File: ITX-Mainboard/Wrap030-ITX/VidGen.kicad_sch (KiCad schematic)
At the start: 26 parts, among them J1 Conn_02x05_Odd_Even, X2 25.175M

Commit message: Schematic substantial completion
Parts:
- added J3: DE15_Receptacle_HighDensity_MountingHoles, Wrap030-ITX:DE15-HD, symbol Connector:DE15_Receptacle_HighDensity_MountingHoles
- C1: footprint Capacitor_SMD:C_0805_2012Metric -> Capacitor_SMD:C_0402_1005Metric_Pad0.74x0.62mm_HandSolder; JLC-Part (none) -> https://jlcpcb.com/partdetail/1877-CL05B104KO5NNNC/C1525
- C15: footprint Capacitor_SMD:C_0805_2012Metric -> Capacitor_SMD:C_0402_1005Metric_Pad0.74x0.62mm_HandSolder; JLC-Part (none) -> https://jlcpcb.com/partdetail/53938-CL05A105KA5NQNC/C52923
- J1: footprint (none) -> Connector_PinHeader_2.54mm:PinHeader_2x05_P2.54mm_Vertical
- RN1, RN2, RN3, RN4, RN5, RN6: Mouser-Part (none) -> 603-YC164-FR-071KL; Notes (none) -> 1k x4
- RN7: Mouser-Part (none) -> 603-YC164-FR-0775RL; Notes (none) -> 75R x4
- VRAM1, VRAM2: footprint Package_DIP:DIP-28_W15.24mm -> Package_DIP:DIP-28_W7.62mm_Socket
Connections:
- net GND: now also J3.10, J3.5, J3.6, J3.7, J3.8
- net VID-B-OUT: now also J3.3
- net VID-G-OUT: now also J3.2
- net VID-H: now also J3.13
- net VID-R-OUT: now also J3.1
- net VID-V: now also J3.14
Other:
- moved on the sheet: J1

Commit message: PCB substantial completion
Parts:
- removed J1: Conn_02x05_Odd_Even, Connector_PinHeader_2.54mm:PinHeader_2x05_P2.54mm_Vertical, symbol Connector_Generic:Conn_02x05_Odd_Even
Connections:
- net GND: now also J3.0
- net VID-B-F: now also VBUF1.13 (IN4_N), VBUF1.14 (OUT4)
- net VID-G-F: now also VBUF1.8 (OUT3), VBUF1.9 (IN3_N)
- net VID-R-F: now also VBUF1.6 (IN2_N), VBUF1.7 (OUT2)
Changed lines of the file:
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@@
   (junction (at 226.06 152.4) (diameter 0) (color 0 0 0 0)
   )
-  (junction (at 231.14 110.49) (diameter 0) (color 0 0 0 0)
-  )
   (junction (at 54.61 154.94) (diameter 0) (color 0 0 0 0)
   )
@@
   (junction (at 54.61 152.4) (diameter 0) (color 0 0 0 0)
   )
-  (junction (at 231.14 105.41) (diameter 0) (color 0 0 0 0)
-  )
   (junction (at 193.04 121.92) (diameter 0) (color 0 0 0 0)
   )
@@
   (junction (at 54.61 147.32) (diameter 0) (color 0 0 0 0)
   )
-  (junction (at 231.14 113.03) (diameter 0) (color 0 0 0 0)
-  )
   (junction (at 195.58 27.94) (diameter 0) (color 0 0 0 0)
   )
   (junction (at 54.61 144.78) (diameter 0) (color 0 0 0 0)
   )
-  (junction (at 231.14 107.95) (diameter 0) (color 0 0 0 0)
-  )
   (junction (at 193.04 104.14) (diameter 0) (color 0 0 0 0)
   )
@@
     (stroke (width 0) (type default))
   )
-  (wire (pts (xy 231.14 110.49) (xy 233.68 110.49))
-    (stroke (width 0) (type default))
-  )
   (wire (pts (xy 195.58 38.1) (xy 220.98 38.1))
     (stroke (width 0) (type default))
   )
-  (wire (pts (xy 246.38 113.03) (xy 259.08 113.03))
-    (stroke (width 0) (type default))
-  )
   (wire (pts (xy 114.3 40.64) (xy 127 40.64))
     (stroke (width 0) (type default))
@@
     (stroke (width 0) (type default))
   )
-  (wire (pts (xy 246.38 105.41) (xy 259.08 105.41))
-    (stroke (width 0) (type default))
-  )
   (wire (pts (xy 152.4 91.44) (xy 165.1 91.44))
     (stroke (width 0) (type default))
@@
     (stroke (width 0) (type default))
   )
-  (wire (pts (xy 231.14 110.49) (xy 231.14 113.03))
-    (stroke (width 0) (type default))
-  )
   (wire (pts (xy 193.04 119.38) (xy 195.58 119.38))
     (stroke (width 0) (type default))
@@
     (stroke (width 0) (type default))
   )
-  (wire (pts (xy 231.14 105.41) (xy 231.14 107.95))
-    (stroke (width 0) (type default))
-  )
   (wire (pts (xy 82.55 76.2) (xy 97.79 76.2))
     (stroke (width 0) (type default))
@@
     (stroke (width 0) (type default))
   )
-  (wire (pts (xy 231.14 105.41) (xy 233.68 105.41))
-    (stroke (width 0) (type default))
-  )
   (wire (pts (xy 259.08 144.78) (xy 251.46 144.78))
     (stroke (width 0) (type default))
   )
-  (wire (pts (xy 231.14 107.95) (xy 231.14 110.49))
-    (stroke (width 0) (type default))
-  )
   (wire (pts (xy 182.88 144.78) (xy 175.26 144.78))
     (stroke (width 0) (type default))
@@
     (stroke (width 0) (type default))
   )
-  (wire (pts (xy 231.14 113.03) (xy 233.68 113.03))
-    (stroke (width 0) (type default))
-  )
   (wire (pts (xy 54.61 149.86) (xy 54.61 152.4))
     (stroke (width 0) (type default))
@@
     (stroke (width 0) (type default))
   )
-  (wire (pts (xy 246.38 110.49) (xy 259.08 110.49))
-    (stroke (width 0) (type default))
-  )
   (wire (pts (xy 195.58 63.5) (xy 195.58 55.88))
     (stroke (width 0) (type default))
@@
     (stroke (width 0) (type default))
   )
-  (wire (pts (xy 233.68 102.87) (xy 231.14 102.87))
-    (stroke (width 0) (type default))
-  )
   (bus (pts (xy 100.33 99.06) (xy 100.33 101.6))
     (stroke (width 0) (type default))
   )
-  (wire (pts (xy 231.14 113.03) (xy 231.14 115.57))
-    (stroke (width 0) (type default))
-  )
   (wire (pts (xy 82.55 48.26) (xy 95.25 48.26))
     (stroke (width 0) (type default))
@@
     (stroke (width 0) (type default))
   )
-  (wire (pts (xy 246.38 107.95) (xy 259.08 107.95))
-    (stroke (width 0) (type default))
-  )
   (wire (pts (xy 114.3 86.36) (xy 127 86.36))
     (stroke (width 0) (type default))
@@
     (stroke (width 0) (type default))
   )
-  (wire (pts (xy 246.38 102.87) (xy 259.08 102.87))
-    (stroke (width 0) (type default))
-  )
   (wire (pts (xy 152.4 35.56) (xy 165.1 35.56))
     (stroke (width 0) (type default))
@@
     (stroke (width 0) (type default))
   )
-  (wire (pts (xy 231.14 102.87) (xy 231.14 105.41))
-    (stroke (width 0) (type default))
-  )
   (wire (pts (xy 213.36 152.4) (xy 226.06 152.4))
     (stroke (width 0) (type default))
@@
     (stroke (width 0) (type default))
   )
-  (wire (pts (xy 231.14 107.95) (xy 233.68 107.95))
-    (stroke (width 0) (type default))
-  )
   (wire (pts (xy 82.55 66.04) (xy 97.79 66.04))
     (stroke (width 0) (type default))
@@
     (effects (font (size 1.27 1.27)) (justify left bottom))
   )
-  (label "VID-V" (at 259.08 102.87 180) (fields_autoplaced)
-    (effects (font (size 1.27 1.27)) (justify right bottom))
-  )
-  (label "VID-R-OUT" (at 259.08 113.03 180) (fields_autoplaced)
-    (effects (font (size 1.27 1.27)) (justify right bottom))
-  )
   (label "~{VID_CS0}" (at 44.45 83.82 0) (fields_autoplaced)
     (effects (font (size 1.27 1.27)) (justify left bottom))
@@
     (effects (font (size 1.27 1.27)) (justify left bottom))
   )
-  (label "VID-B-OUT" (at 259.08 107.95 180) (fields_autoplaced)
-    (effects (font (size 1.27 1.27)) (justify right bottom))
-  )
   (label "VID-B-D" (at 228.6 137.16 0) (fields_autoplaced)
     (effects (font (size 1.27 1.27)) (justify left bottom))
@@
     (effects (font (size 1.27 1.27)) (justify left bottom))
   )
+  (label "VID-G-F" (at 220.98 55.88 180) (fields_autoplaced)
+    (effects (font (size 1.27 1.27)) (justify right bottom))
+  )
   (label "VID_A8" (at 114.3 48.26 0) (fields_autoplaced)
     (effects (font (size 1.27 1.27)) (justify left bottom))
@@
     (effects (font (size 1.27 1.27)) (justify right bottom))
   )
-  (label "VID-H" (at 259.08 105.41 180) (fields_autoplaced)
-    (effects (font (size 1.27 1.27)) (justify right bottom))
-  )
   (label "VID_D0" (at 165.1 83.82 180) (fields_autoplaced)
     (effects (font (size 1.27 1.27)) (justify right bottom))
@@
     (effects (font (size 1.27 1.27)) (justify left bottom))
   )
-  (label "VID-G-OUT" (at 259.08 110.49 180) (fields_autoplaced)
-    (effects (font (size 1.27 1.27)) (justify right bottom))
-  )
   (label "VID_A7" (at 44.45 45.72 0) (fields_autoplaced)
     (effects (font (size 1.27 1.27)) (justify left bottom))
@@
     (effects (font (size 1.27 1.27)) (justify left bottom))
   )
+  (label "VID-B-F" (at 220.98 73.66 180) (fields_autoplaced)
+    (effects (font (size 1.27 1.27)) (justify right bottom))
+  )
   (label "VID_TDI" (at 44.45 119.38 0) (fields_autoplaced)
     (effects (font (size 1.27 1.27)) (justify left bottom))
@@
     (effects (font (size 1.27 1.27)) (justify right bottom))
   )
+  (label "VID-R-F" (at 220.98 38.1 180) (fields_autoplaced)
+    (effects (font (size 1.27 1.27)) (justify right bottom))
+  )
   (label "VID-I-D" (at 95.25 45.72 180) (fields_autoplaced)
     (effects (font (size 1.27 1.27)) (justify right bottom))
@@
     )
   )
-  (symbol (lib_id "Connector_Generic:Conn_02x05_Odd_Even") (at 238.76 107.95 0) (unit 1)
-    (in_bom yes) (on_board yes) (dnp no) (fields_autoplaced)
-    (property "Reference" "J1" (at 240.03 98.5901 0)
-      (effects (font (size 1.27 1.27)))
-    )
-    (property "Value" "Conn_02x05_Odd_Even" (at 240.03 100.5111 0)
-      (effects (font (size 1.27 1.27)))
-    )
-    (property "Footprint" "Connector_PinHeader_2.54mm:PinHeader_2x05_P2.54mm_Vertical" (at 238.76 107.95 0)
-      (effects (font (size 1.27 1.27)) hide)
-    )
-    (property "Datasheet" "~" (at 238.76 107.95 0)
-      (effects (font (size 1.27 1.27)) hide)
-    )
-    (property "JLC-Part" "" (at 238.76 107.95 0)
-      (effects (font (size 1.27 1.27)) hide)
-    )
-    (property "Mouser-Part" "" (at 238.76 107.95 0)
-      (effects (font (size 1.27 1.27)) hide)
-    )
-    (property "Notes" "" (at 238.76 107.95 0)
-      (effects (font (size 1.27 1.27)) hide)
-    )
-    (pin "1")
-    (pin "10")
-    (pin "2")
-    (pin "3")
-    (pin "4")
-    (pin "5")
-    (pin "6")
-    (pin "7")
-    (pin "8")
-    (pin "9")
-    (instances
-      (project "Wrap030-ITX"
-        (path "/911cb688-7d4c-4194-bbd3-2b645bd8d53c/26daa56c-062f-43fe-98ce-9d136969f1f9"
-          (reference "J1") (unit 1)
-        )
-      )
-    )
-  )
   (symbol (lib_id "power:VCC") (at 85.09 134.62 0) (unit 1)
     (in_bom yes) (on_board yes) (dnp no) (fields_autoplaced)
@@
     )
   )
-  (symbol (lib_id "power:GND") (at 231.14 115.57 0) (unit 1)
-    (in_bom yes) (on_board yes) (dnp no) (fields_autoplaced)
-    (property "Reference" "#PWR04" (at 231.14 121.92 0)
-      (effects (font (size 1.27 1.27)) hide)
-    )
-    (property "Value" "GND" (at 231.14 119.7055 0)
-      (effects (font (size 1.27 1.27)))
-    )
-    (property "Footprint" "" (at 231.14 115.57 0)
-      (effects (font (size 1.27 1.27)) hide)
-    )
-    (property "Datasheet" "" (at 231.14 115.57 0)
-      (effects (font (size 1.27 1.27)) hide)
-    )
-    (pin "1")
-    (instances
-      (project "Wrap030-ITX"
-        (path "/911cb688-7d4c-4194-bbd3-2b645bd8d53c"
-          (reference "#PWR04") (unit 1)
-        )
-        (path "/911cb688-7d4c-4194-bbd3-2b645bd8d53c/26daa56c-062f-43fe-98ce-9d136969f1f9"
-          (reference "#PWR089") (unit 1)
-        )
-      )
-    )
-  )
   (symbol (lib_id "power:GND") (at 170.18 93.98 0) (unit 1)
     (in_bom yes) (on_board yes) (dnp no) (fields_autoplaced)
@@
         )
       )
+    )
+  )
+  (symbol (lib_id "power:GND") (at 203.2 129.54 90) (unit 1)
+    (in_bom yes) (on_board yes) (dnp no) (fields_autoplaced)
+    (property "Reference" "#PWR04" (at 209.55 129.54 0)
+      (effects (font (size 1.27 1.27)) hide)
+    )
+    (property "Value" "GND" (at 206.375 129.8568 90)
+      (effects (font (size 1.27 1.27)) (justify right))
+    )
+    (property "Footprint" "" (at 203.2 129.54 0)
+      (effects (font (size 1.27 1.27)) hide)
+    )
+    (property "Datasheet" "" (at 203.2 129.54 0)
+      (effects (font (size 1.27 1.27)) hide)
+    )
+    (pin "1")
+    (instances
+      (project "Wrap030-ITX"
+        (path "/911cb688-7d4c-4194-bbd3-2b645bd8d53c"
+          (reference "#PWR04") (unit 1)
+        )
+        (path "/911cb688-7d4c-4194-bbd3-2b645bd8d53c/26daa56c-062f-43fe-98ce-9d136969f1f9"
+          (reference "#PWR089") (unit 1)
+        )
+      )

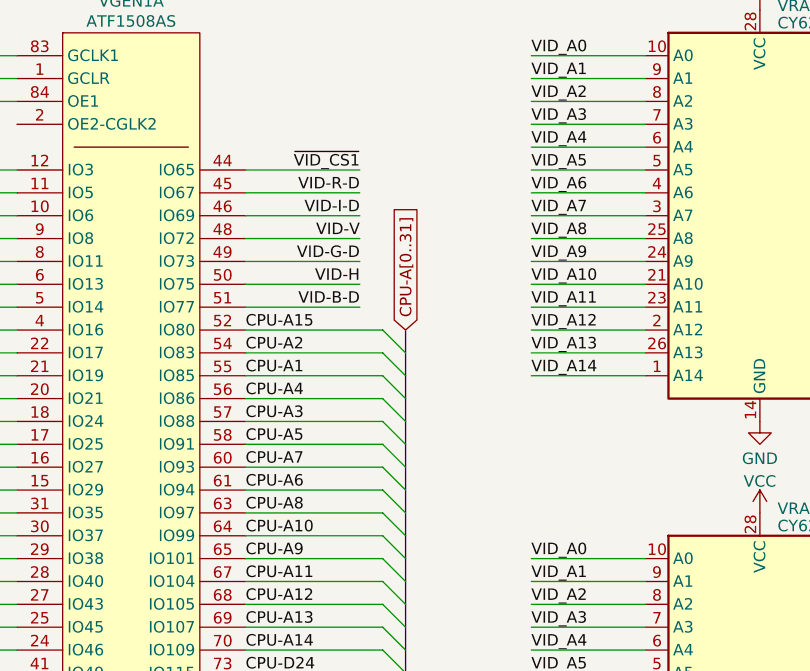
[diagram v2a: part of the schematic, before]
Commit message: Add interrupt controller to schematic
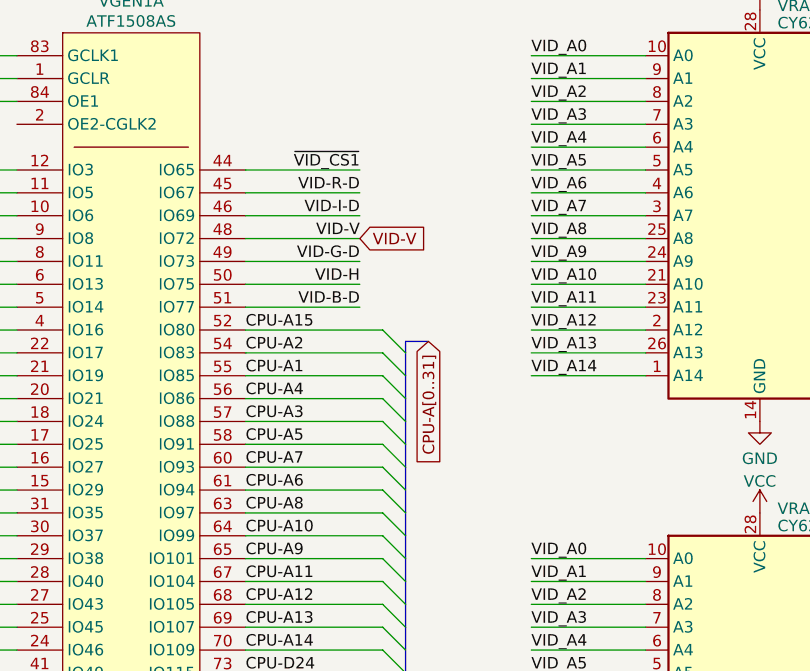
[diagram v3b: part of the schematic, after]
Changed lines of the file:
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@@
+    (stroke (width 0) (type default))
+  )
+  (bus (pts (xy 102.87 59.69) (xy 100.33 59.69))
     (stroke (width 0) (type default))
   )
@@
     (stroke (width 0) (type default))
   )
+  (bus (pts (xy 100.33 59.69) (xy 100.33 60.96))
+    (stroke (width 0) (type default))
+  )
   (wire (pts (xy 218.44 25.4) (xy 231.14 25.4))
     (stroke (width 0) (type default))
@@
   )
   (wire (pts (xy 264.16 137.16) (xy 264.16 139.7))
-    (stroke (width 0) (type default))
-  )
-  (bus (pts (xy 100.33 58.42) (xy 100.33 60.96))
     (stroke (width 0) (type default))
   )
@@
     )
   )
-  (global_label "CPU-A[0..31]" (shape input) (at 100.33 58.42 90) (fields_autoplaced)
-    (effects (font (size 1.27 1.27)) (justify left))
-    (property "Intersheetrefs" "${INTERSHEET_REFS}" (at 100.33 42.4512 90)
-      (effects (font (size 1.27 1.27)) (justify left) hide)
+  (global_label "CPU-A[0..31]" (shape input) (at 102.87 59.69 270) (fields_autoplaced)
+    (effects (font (size 1.27 1.27)) (justify right))
+    (property "Intersheetrefs" "${INTERSHEET_REFS}" (at 102.87 75.6588 90)
+      (effects (font (size 1.27 1.27)) (justify right) hide)
     )
   )
@@
     )
   )
+  (global_label "VID-V" (shape input) (at 95.25 48.26 0) (fields_autoplaced)
+    (effects (font (size 1.27 1.27)) (justify left))
+    (property "Intersheetrefs" "${INTERSHEET_REFS}" (at 103.7802 48.26 0)
+      (effects (font (size 1.27 1.27)) (justify left) hide)
+    )
+  )

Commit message: Completing PCB Routing
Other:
- title: Wrap030 ITX -> Wrap030-ATX Mainboard
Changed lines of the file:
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@@
   (paper "USLetter")
   (title_block
-    (title "Wrap030 ITX")
-    (date "2023-03-15")
-    (rev "0")
+    (title "Wrap030-ATX Mainboard")
+    (date "2023-03-26")
+    (rev "1")
     (company "techav")
   )
